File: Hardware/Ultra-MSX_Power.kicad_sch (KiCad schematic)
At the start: 70 parts, among them J10-0 ATX-24-LRJ, J10-1 Conn_KLDX-0202-A, U1 MPU_Z380, U10 SST39SF040, U14 SN74ABTH16244DL, U15 SN74ABT241APW, U2 AT40K20-2EQJ, U4 YM2610, U5 BQ4802YPW, U6 74ABT245PW_118, U8 AS6C4008-55STIN, U9 DAC_YM3016

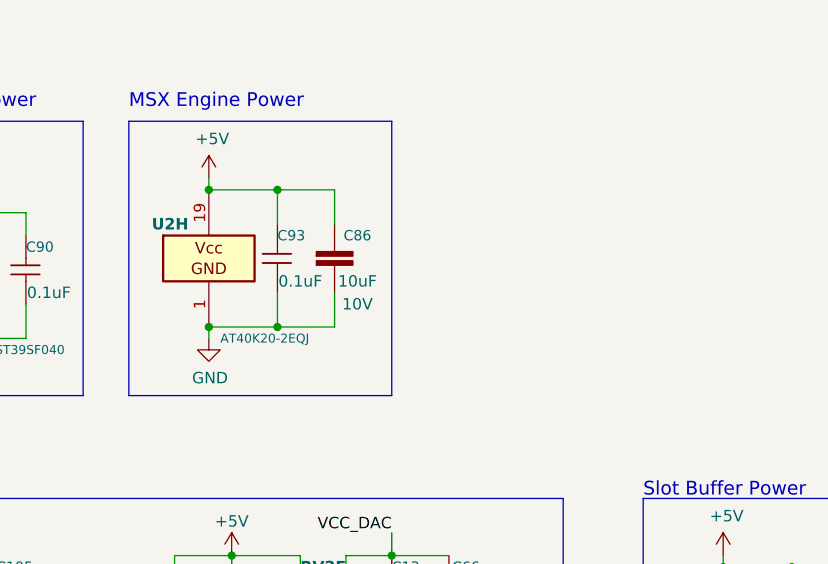
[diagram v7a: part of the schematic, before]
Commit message: Multiple redesigns of the IO-shield. Replaced FPGA with lower pin-count AT10K, since the higher pin-count one is now obsolete.
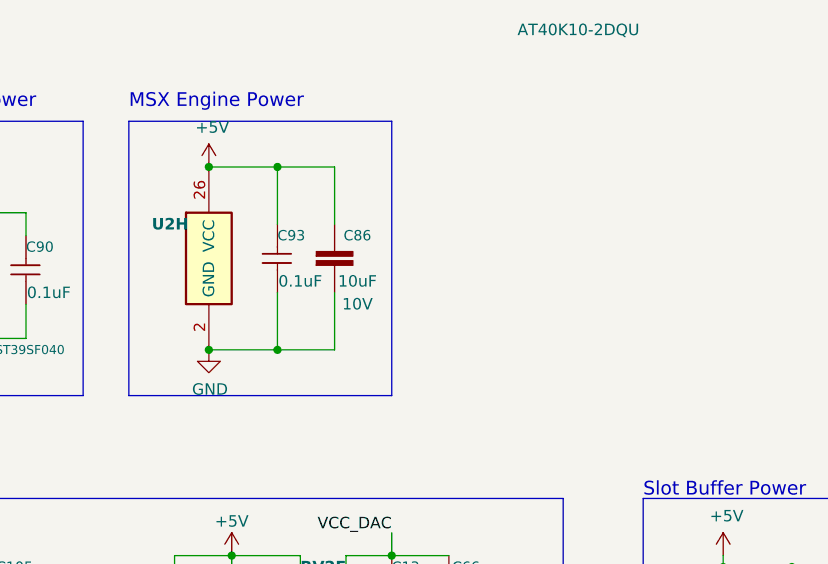
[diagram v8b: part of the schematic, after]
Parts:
- C1, C103, C104, C13, C22, C3, C36, C37, C59, C63, C7, C74, C8, C88, C9, C90, C92, C93, C94, C95, C97, C98: Price €0,14 -> (none)
- U2: value AT40K20-2EQJ -> AT40K10-2DQU; footprint Package_QFP:PQFP-240_32.1x32.1mm_P0.5mm -> Package_QFP:PQFP-208_28x28mm_P0.5mm; symbol LRJ-parts:AT40K20-2EQJ -> LRJ-parts:AT40K10-2DQU; MPN AT40K20-2EQJ -> AT40K10-2DQU; Manufacturer (none) -> Microchip/ATmel; Manufacturer_Name Microchip -> (none); Status (none) -> Active
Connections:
- net +5V: now also U2.106 (VCC), U2.130 (VCC), U2.154 (VCC), U2.183 (VCC), U2.205 (VCC), U2.26 (VCC), U2.55 (VCC), U2.78 (VCC); no longer U2.101 (VCC), U2.121 (VCC), U2.140 (VCC), U2.150 (VCC), U2.161 (VCC), U2.180 (VCC), U2.19 (VCC), U2.201 (VCC), U2.212 (VCC), U2.222 (VCC), U2.240 (VCC), U2.30 (VCC), U2.40 (VCC), U2.61 (VCC), U2.80 (VCC), U2.90 (VCC)
- net GND: now also U2.101 (GND), U2.131 (GND), U2.142 (GND), U2.160 (GND), U2.171 (GND), U2.194 (GND), U2.2 (GND), U2.25 (GND), U2.37 (GND), U2.49 (GND), U2.67 (GND), U2.79 (GND), U2.90 (GND); no longer U2.1 (GND), U2.106 (GND), U2.135 (GND), U2.151 (GND), U2.166 (GND), U2.196 (GND), U2.211 (GND), U2.227 (GND), U2.29 (GND), U2.45 (GND), U2.59 (GND), U2.75 (GND), U2.91 (GND)
- net +3V3 renamed +3.3V
- new net: U2.1 (N/C), U2.102 (N/C), U2.104 (N/C), U2.105 (N/C), U2.107 (N/C), U2.155 (N/C), U2.156 (N/C), U2.157 (N/C), U2.158 (N/C), U2.206 (N/C), U2.207 (N/C), U2.208 (N/C), U2.3 (N/C), U2.51 (N/C), U2.52 (N/C), U2.53 (N/C), U2.54 (N/C)
